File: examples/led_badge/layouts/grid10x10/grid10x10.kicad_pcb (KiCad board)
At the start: 4 copper layers, 200 parts

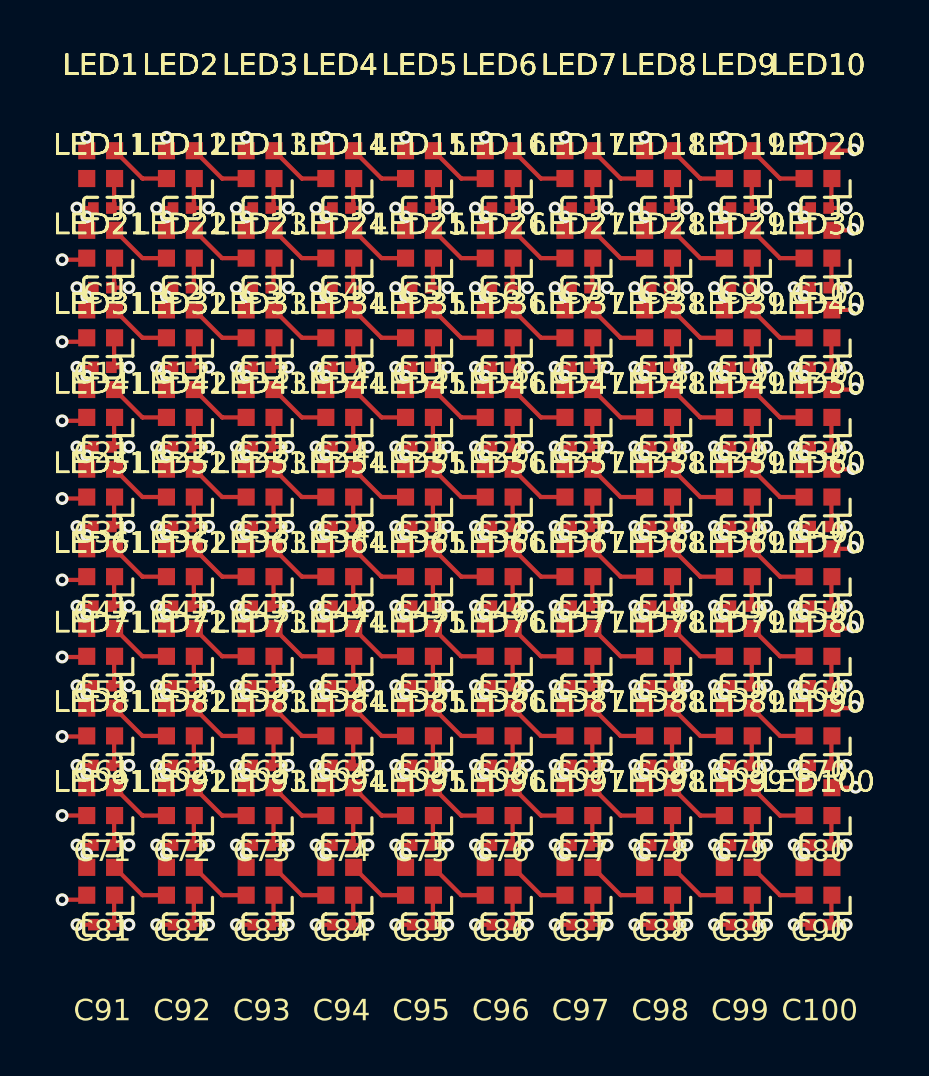
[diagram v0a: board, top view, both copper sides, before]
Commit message: Restore Atopile Local 0.2 on pinned 0.15.9 sources
Import the publicly distributed atopile 0.15.9 PyPI source release as the
compiler/UI baseline, retaining upstream main as its historical parent.
PyPI source SHA256: 681cc1e123646dd133de31b631aedaf4eaac88682613b4f82d1da4b3ef8b4e8e.

Revive the local VS Code extension with a separate identity and launcher,
isolated state, bundled visualization assets, and provider settings. Bridge
the existing Atopile tool harness to a natively signed-in Codex app-server
for ChatGPT-plan use, retaining direct API providers as explicit options.
Include local part import, layout tools, packaging/runtime setup and tests.

Preserve upstream licensing, restored GitHub metadata and source notices.
Exclude local environments, generated webview bundles and personal QA paths.
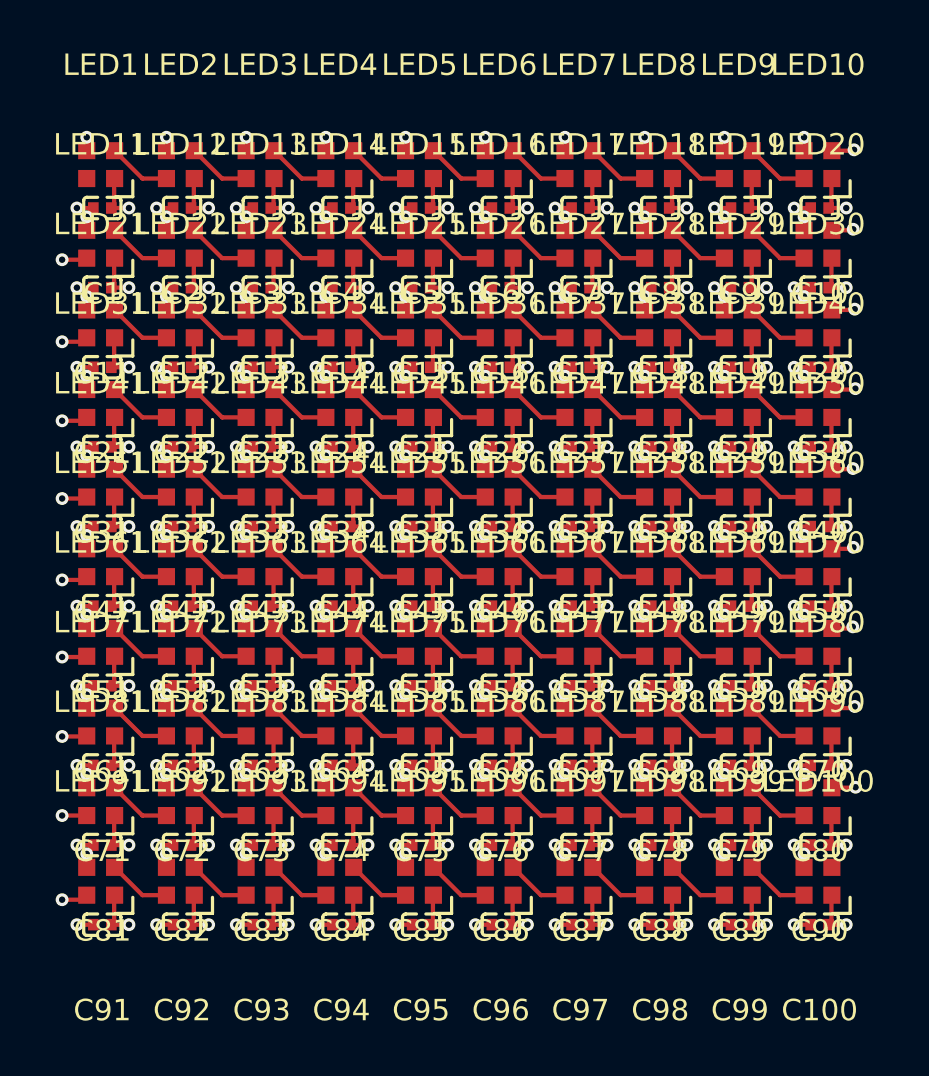
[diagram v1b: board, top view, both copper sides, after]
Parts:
- C1, C10, C100, C11, C12, C13, C14, C15, C16, C17, C18, C19, C2, C20, C21, C22, C23, C24, C25, C26, C27, C28, C29, C3, C30, C31, C32, C33, C34, C35, C36, C37, C38, C39, C4, C40, C41, C42, C43, C44, C45, C46, C47, C48, C49, C5, C50, C51, C52, C53, C54, C55, C56, C57, C58, C59, C6, C60, C61, C62, C63, C64, C65, C66, C67, C68, C69, C7, C70, C71, C72, C73, C74, C75, C76, C77, C78, C79, C8, C80, C81, C82, C83, C84, C85, C86, C87, C88, C89, C9, C90, C91, C92, C93, C94, C95, C96, C97, C98, C99: value 100nF -> 100nF ±10%
